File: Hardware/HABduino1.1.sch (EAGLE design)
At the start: 40 parts, among them IC2 TPS61201, U1 ARDUINO_SHIELDNO_SILK, U2 LM3480IM3-3.3, U3 TXS0102DCTT

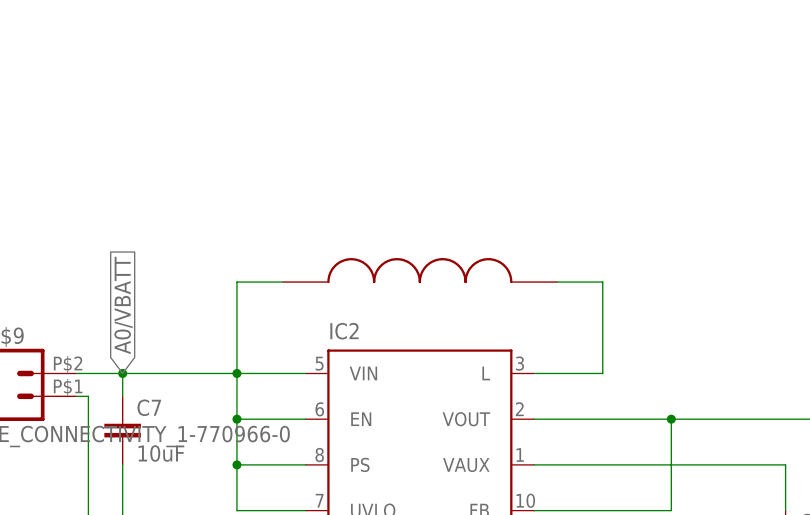
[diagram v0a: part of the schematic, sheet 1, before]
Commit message: Updated BRD File + Added Sketchup Model
1/ Removed GND via that linked VCC to GND (duh!)
2/ Cleaned up silk screen.
3/ Added location mark to TPS61200 module.
4/ Added Sketchup Model
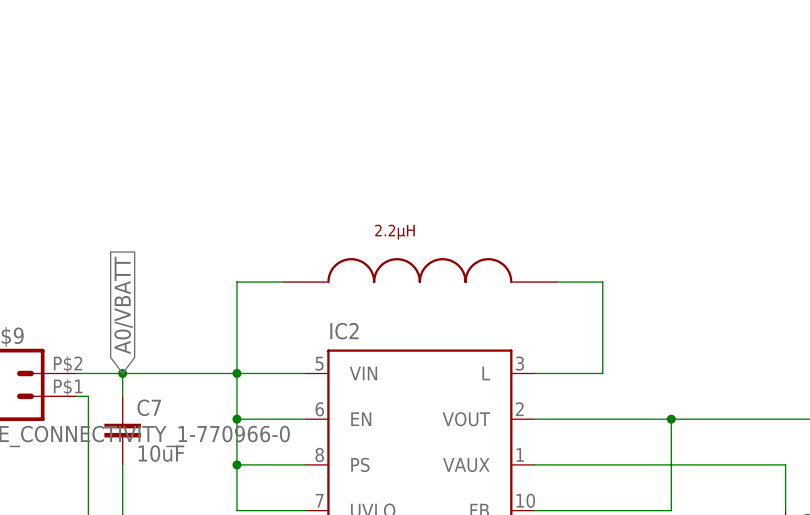
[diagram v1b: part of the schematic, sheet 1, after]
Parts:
- U$10: value (none) -> 2.2µH
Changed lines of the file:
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@@
 <attribute name="FARNELL" value="1098556"/>
 </part>
-<part name="U$10" library="StevesCoilCraft" deviceset="COILCRAFT_LPS4018" device=""/>
+<part name="U$10" library="StevesCoilCraft" deviceset="COILCRAFT_LPS4018" device="" value="2.2µH"/>
 </parts>
 <sheets>
